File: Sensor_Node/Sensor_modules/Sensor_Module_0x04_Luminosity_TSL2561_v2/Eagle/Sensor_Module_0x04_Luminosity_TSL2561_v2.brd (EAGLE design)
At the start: 55 x 35 mm, 20 parts, among them J1 M04_SMD_90, J4 ARDUINO_ISP, U2 ATMEGA328P_TQFP, U3 MIKE-TEMP_TSL2561T, Y1 8MHZ

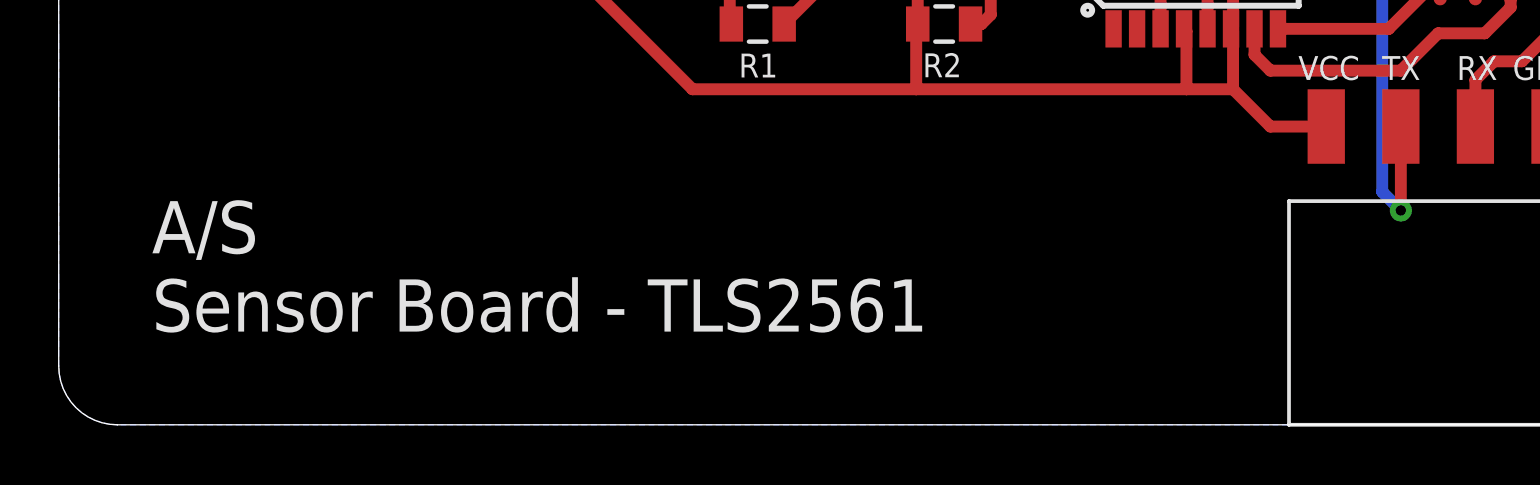
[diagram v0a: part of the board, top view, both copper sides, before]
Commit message: Renaming boards to modules inside eagle files
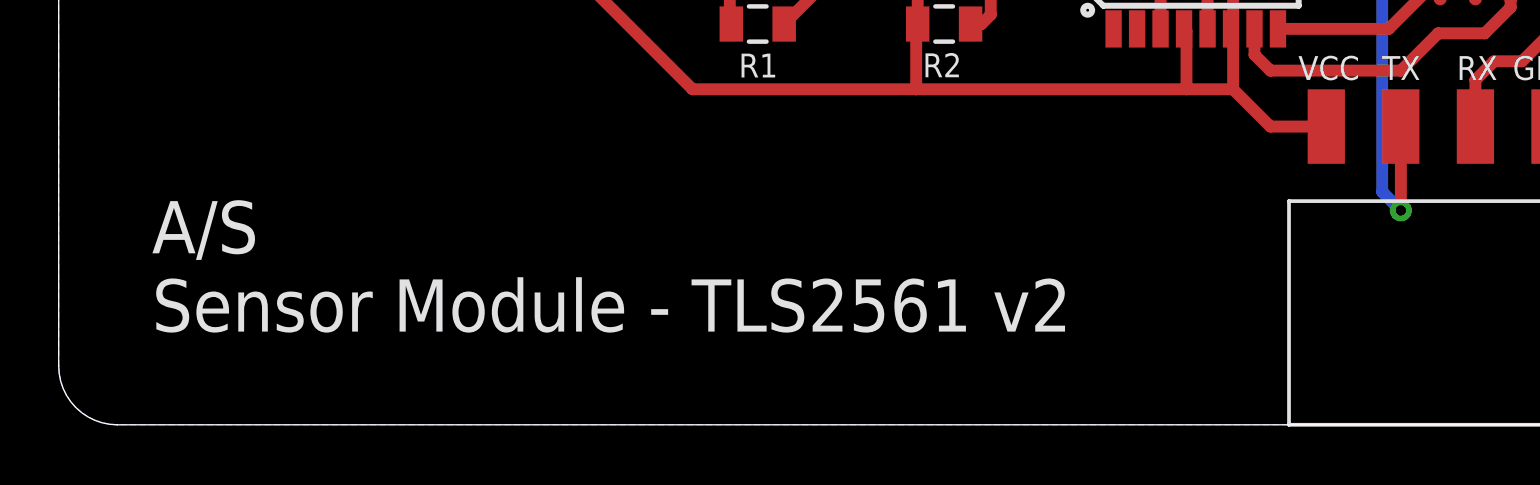
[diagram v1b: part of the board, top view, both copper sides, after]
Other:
- board text added: "A/S Sensor Module - TLS2561 v2"
- board text removed: "A/S Sensor Board - TLS2561"
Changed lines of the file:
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@@
 <?xml version="1.0" encoding="utf-8"?>
 <!DOCTYPE eagle SYSTEM "eagle.dtd">
-<eagle version="8.5.2">
+<eagle version="9.1.1">
 <drawing>
 <settings>
@@
 <text x="49.53" y="11.7475" size="0.8128" layer="21">GND</text>
 <text x="3.175" y="3.175" size="1.778" layer="21">A/S
-Sensor Board - TLS2561</text>
+Sensor Module - TLS2561 v2</text>
 <circle x="52.07" y="31.115" radius="1.309084375" width="0.4064" layer="21"/>
 <text x="53.853340625" y="26.9864" size="0.8128" layer="21" rot="R270">VCC</text>
@@
 <param name="checkStop" value="0"/>
 <param name="checkValues" value="0"/>
+<param name="checkNames" value="1"/>
+<param name="checkWireStubs" value="1"/>
+<param name="checkPolygonWidth" value="0"/>
 <param name="useDiameter" value="13"/>
 <param name="maxErrors" value="50"/>
@@
 </signal>
 </signals>
+<mfgpreviewcolors>
+<mfgpreviewcolor name="soldermaskcolor" color="0xC8008000"/>
+<mfgpreviewcolor name="silkscreencolor" color="0xFFFEFEFE"/>
+<mfgpreviewcolor name="backgroundcolor" color="0xFF282828"/>
+<mfgpreviewcolor name="coppercolor" color="0xFFFFBF00"/>
+<mfgpreviewcolor name="substratecolor" color="0xFF786E46"/>
+</mfgpreviewcolors>
 </board>
 </drawing>
